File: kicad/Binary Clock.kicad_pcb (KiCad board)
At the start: 2 copper layers, 162.6 x 101.6 mm, 54 parts, among them J1 AVR-ISP-10, J2 UART, J3 COM/TWI, SW1 INC_HOUR, SW2 INC_MINUTE, SW3 INC_SECOND, SW4 INC_BTNESS, U1 PCF8583P, U2 ATmega32A-PU, Y1 32768hZ

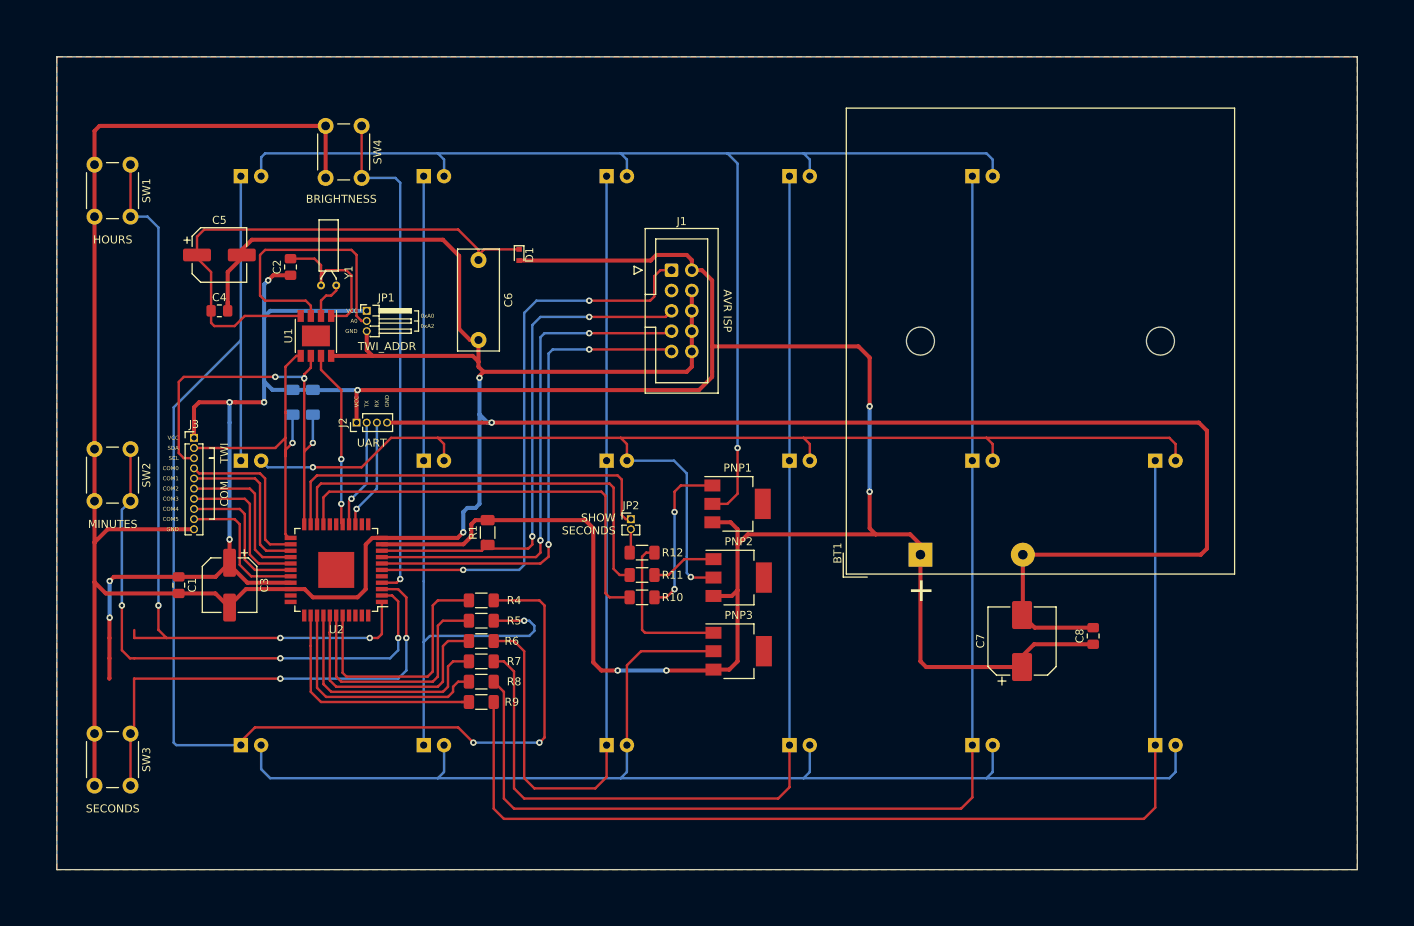
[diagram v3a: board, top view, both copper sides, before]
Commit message: Add support for buzzer
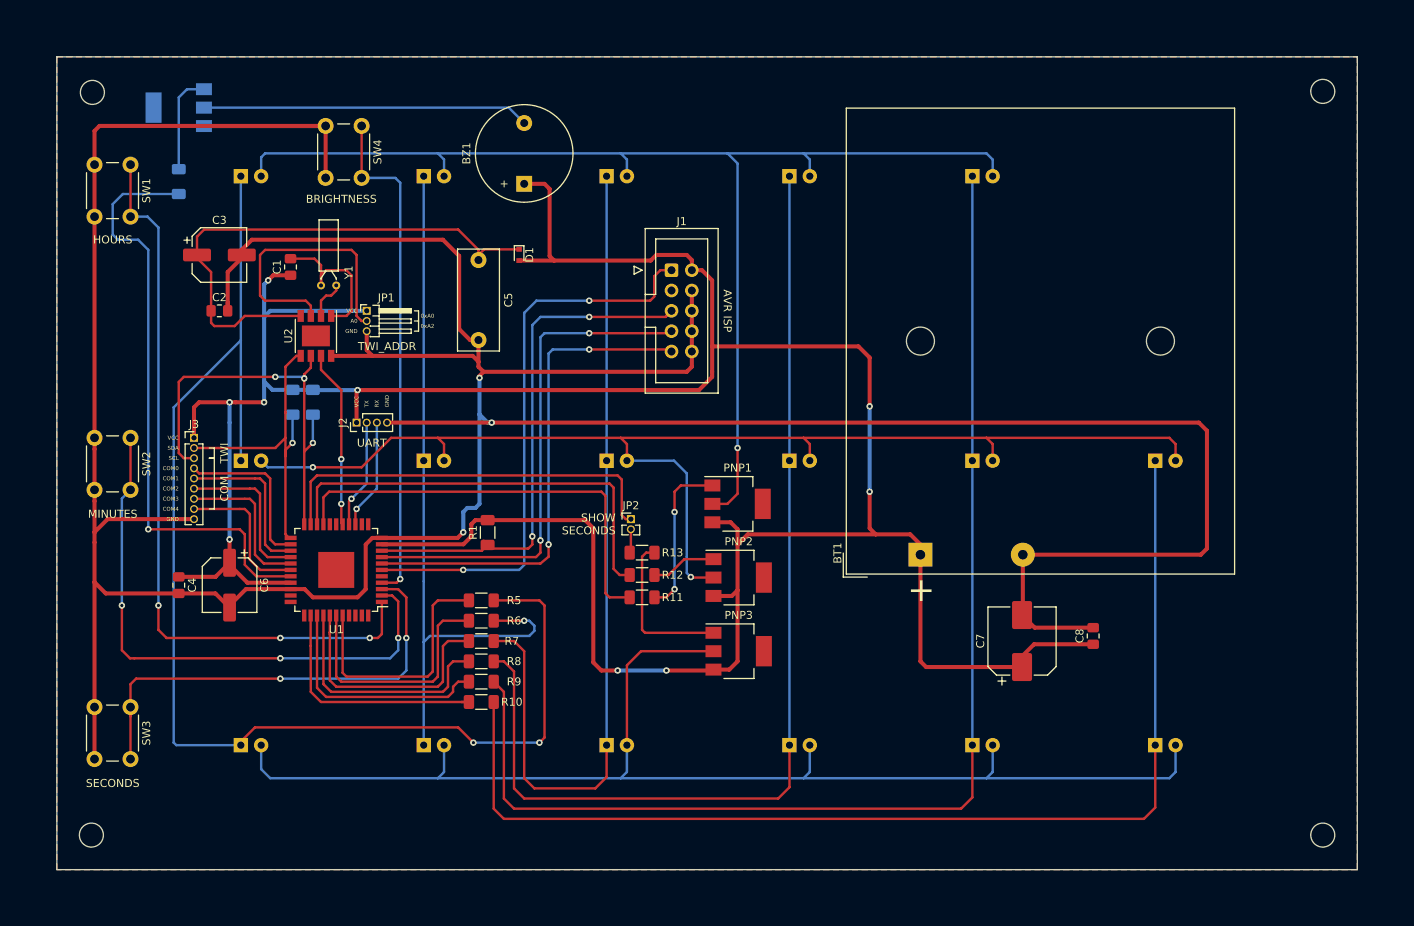
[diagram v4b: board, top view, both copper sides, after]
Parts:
- removed the C3 at (87.6, 121.9)
- added BZ1: Buzzer, Buzzer_Beeper:Buzzer_12x9.5RM7.6, F.Cu at (124.5, 71.8)
- added C6: 22u, Capacitor_SMD:CP_Elec_6.3x5.3, F.Cu at (87.6, 121.9)
- added NPN1: Q_NPN_BCE, Package_TO_SOT_SMD:SOT-223, B.Cu at (81.3, 62.2)
- added R4: 2k2, Resistor_SMD:R_1206_3216Metric_Pad1.30x1.75mm_HandSolder, B.Cu at (81.3, 71.5)
- added REF**: MountingHole_3mm, MountingHole:MountingHole_3mm, F.Cu at (224.3, 60.2)
- added REF**: MountingHole_3mm, MountingHole:MountingHole_3mm, F.Cu at (224.3, 153.2)
- added REF**: MountingHole_3mm, MountingHole:MountingHole_3mm, F.Cu at (70.4, 153.2)
- added REF**: MountingHole_3mm, MountingHole:MountingHole_3mm, F.Cu at (70.5, 60.3)
- J3: value COM/TWI -> COM/TW; footprint Connector_PinHeader_1.27mm:PinHeader_1x10_P1.27mm_Vertical -> Connector_PinHeader_1.27mm:PinHeader_1x09_P1.27mm_Vertical
- moved SW3 3.32 mm to (75.2, 137.2)
- moved SW2 1.41 mm to (75.2, 103.5)
- renumbered C2 to C1, C4 to C2, C5 to C3, C1 to C4, C6 to C5, R9 to R10, R10 to R11, R11 to R12, R12 to R13, R4 to R5, R5 to R6, R6 to R7, R7 to R8, R8 to R9, U2 to U1, U1 to U2
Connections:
- J3 pad 9: /COM5 -> GND
- U1 pad 29: /COM5 -> /BUZZER
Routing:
- net /BUZZER: track 0.00 -> 75.2 mm, vias 0 -> 1
- net Net-(BZ1-Pad2): track 0.00 -> 42.1 mm
- net /COM5: track 18.0 -> 0.00 mm
- net Net-(NPN1-Pad1): track 0.00 -> 12.5 mm
- net GND: track 480.6 -> 492.6 mm
- net VCC: track 394.9 -> 386.4 mm, vias 11 -> 9
- net /INC_HOUR: track 98.4 -> 93.4 mm
- net /INC_SECOND: track 60.6 -> 57.2 mm
- net /INC_MINUTE: track 69.4 -> 70.8 mm
- added copper zone on B.Cu, net (none)
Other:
- board text removed: "COM5"

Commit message: Change goldpins to 2.56mm
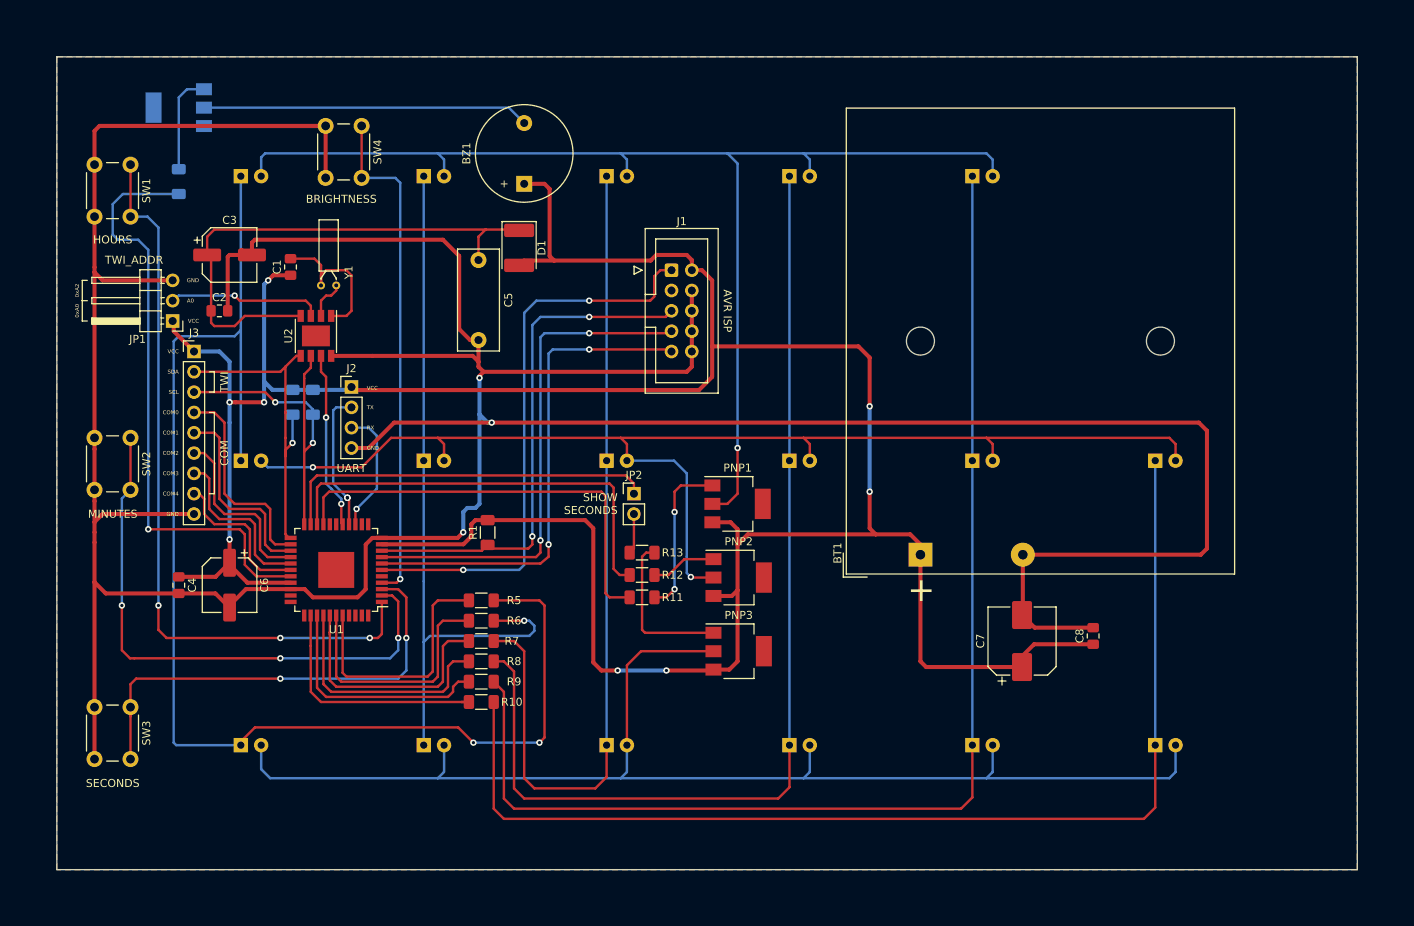
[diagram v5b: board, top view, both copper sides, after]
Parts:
- removed REF** (x4): MountingHole_3mm, MountingHole:MountingHole_3mm
- D1: footprint Diode_SMD:D_SOD-523 -> Diode_SMD:D_2114_3652Metric
- J2: footprint Connector_PinHeader_1.27mm:PinHeader_1x04_P1.27mm_Vertical -> Connector_PinHeader_2.54mm:PinHeader_1x04_P2.54mm_Vertical
- J3: footprint Connector_PinHeader_1.27mm:PinHeader_1x09_P1.27mm_Vertical -> Connector_PinHeader_2.54mm:PinHeader_1x09_P2.54mm_Vertical
- JP1: footprint Connector_PinHeader_1.27mm:PinHeader_1x03_P1.27mm_Horizontal -> Connector_PinHeader_2.54mm:PinHeader_1x03_P2.54mm_Horizontal
- JP2: footprint Connector_PinHeader_1.27mm:PinHeader_1x02_P1.27mm_Vertical -> Connector_PinHeader_2.54mm:PinHeader_1x02_P2.54mm_Vertical
- moved JP1 24.3 mm to (80.5, 88.9), turned to 180 degrees
- moved J3 10.8 mm to (83.2, 92.7)
- moved J2 4.49 mm to (102.9, 97.2), turned to 0 degrees
- moved JP2 3.20 mm to (138.2, 110.5)
- moved C3 1.27 mm to (87.6, 80.6)
- moved D1 0.89 mm to (123.8, 79.8)
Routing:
- net Net-(JP1-Pad2): track 35.0 -> 19.2 mm, vias 0 -> 1
- net GND: track 492.6 -> 506.4 mm
- net /SCL: track 53.9 -> 42.9 mm, vias 3 -> 2
- net VCC: track 386.4 -> 376.2 mm, vias 9 -> 8
- net /COM0: track 20.5 -> 26.3 mm
- net Net-(HD1-Pad1): track 162.0 -> 167.4 mm
- net /COM1: track 20.3 -> 24.9 mm
- net /TX: track 13.6 -> 17.5 mm, vias 1 -> 2
- net /COM2: track 19.7 -> 22.7 mm
- net /SECOND_LED: track 50.5 -> 47.8 mm
- net Net-(JP2-Pad2): track 3.02 -> 5.26 mm
- net /COM3: track 19.2 -> 21.2 mm
- net /RX: track 13.8 -> 15.8 mm
- net /COM4: track 18.6 -> 19.4 mm

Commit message: Update PCB footprints
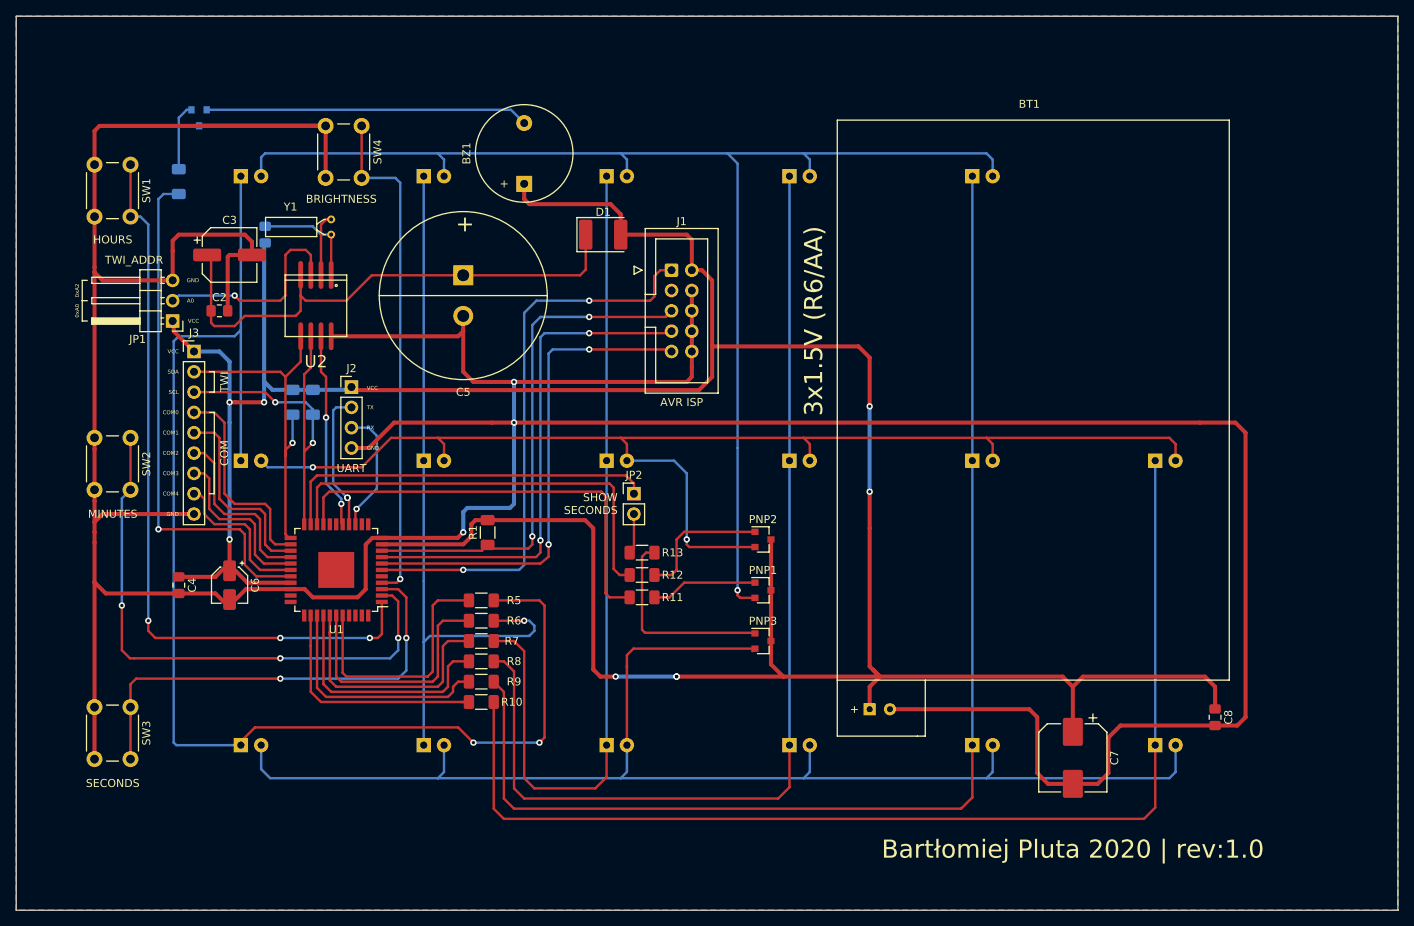
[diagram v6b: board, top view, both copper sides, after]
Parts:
- BT1: footprint Battery:BatteryHolder_TruPower_BH-331P_3xAA -> Project Footprints:BatteryPackage
- C1: moved to B.Cu
- C5: footprint Capacitor_THT:C_Disc_D12.5mm_W5.0mm_P10.00mm -> Project Footprints:SuperCapacitor
- C6: footprint Capacitor_SMD:CP_Elec_6.3x5.3 -> Capacitor_SMD:CP_Elec_4x3
- NPN1, PNP1, PNP2, PNP3: footprint Package_TO_SOT_SMD:SOT-223 -> Package_TO_SOT_SMD:SOT-23
- U2: footprint Package_SO:Diodes_SO-8EP -> PCF8583:SOT176-1
- moved BT1 25.0 mm to (188.6, 97.8), turned to 0 degrees
- moved C8 18.3 mm to (210.8, 138.4), turned to 270 degrees
- moved C7 15.9 mm to (193.0, 143.5), turned to 270 degrees
- moved PNP1 11.3 mm to (154.3, 122.6)
- moved D1 10.6 mm to (134.3, 78.1), turned to 0 degrees
- moved Y1 8.28 mm to (100.3, 76.2), turned to 270 degrees
- moved PNP2 5.65 mm to (154.3, 116.2)
- moved C1 5.14 mm to (92.1, 78.1)
- moved C5 4.84 mm to (116.8, 85.7)
- moved U2 3.77 mm to (98.4, 87.0), turned to 180 degrees
- moved PNP3 3.29 mm to (154.3, 128.9)
- moved NPN1 2.84 mm to (83.8, 63.5), turned to 270 degrees
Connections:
- J1 pad 3: Net-(J1-Pad3) -> (no net)
- U1 pad 12: Net-(U1-Pad12) -> (no net)
- U1 pad 13: Net-(U1-Pad13) -> (no net)
- U1 pad 17: Net-(U1-Pad17) -> (no net)
- U1 pad 18: Net-(U1-Pad18) -> (no net)
- U1 pad 32: Net-(U1-Pad32) -> (no net)
- U1 pad 33: Net-(U1-Pad33) -> (no net)
- U1 pad 34: Net-(U1-Pad34) -> (no net)
- U1 pad 5: Net-(U1-Pad5) -> (no net)
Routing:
- net GND: track 506.4 -> 532.5 mm
- net VCC: track 376.2 -> 397.0 mm
- net Net-(HD1-Pad2): track 152.7 -> 164.0 mm
- net /BUZZER: track 75.2 -> 65.3 mm
- net Net-(PNP2-Pad1): track 8.20 -> 17.0 mm
- net Net-(PNP1-Pad1): track 20.2 -> 13.3 mm, vias 2 -> 0
- net Net-(JP1-Pad2): track 19.2 -> 26.0 mm
- net Net-(PNP3-Pad2): track 160.8 -> 167.6 mm
- net Net-(C1-Pad2): track 19.5 -> 13.7 mm
- net Net-(PNP3-Pad1): track 20.0 -> 25.2 mm
- net Net-(NPN1-Pad1): track 12.5 -> 8.43 mm
- net Net-(U2-Pad2): track 4.97 -> 7.84 mm
- net /SCL: track 42.9 -> 45.3 mm
- net /RTC_INT: track 22.2 -> 24.6 mm
- net /SDA: track 41.5 -> 43.6 mm
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- added copper zone on B.Cu, net GND
- removed copper zone on B.Cu, net (none)
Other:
- board size 162.6 x 101.6 mm -> 172.7 x 111.8 mm
- board text added: "3x1.5V (R6/AA)"
- board text added: "Bartłomiej Pluta 2020 | rev:1.0"

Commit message: Fix some issues on PCB
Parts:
- added REF**: MountingHole_2mm, MountingHole:MountingHole_2mm, F.Cu at (160.0, 55.9)
- added REF**: MountingHole_2mm, MountingHole:MountingHole_2mm, F.Cu at (134.6, 55.9)
- added REF**: MountingHole_3mm, MountingHole:MountingHole_3mm, F.Cu at (228.6, 55.9)
- added REF**: MountingHole_3mm, MountingHole:MountingHole_3mm, F.Cu at (228.6, 157.5)
- added REF**: MountingHole_3mm, MountingHole:MountingHole_3mm, F.Cu at (66.0, 157.5)
- added REF**: MountingHole_3mm, MountingHole:MountingHole_3mm, F.Cu at (66.0, 55.9)
- NPN1: value Q_NPN_BCE -> Q_NPN_BEC
- PNP1, PNP2, PNP3: value Q_PNP_BCE -> Q_PNP_BEC
- R10, R5, R6, R7, R8, R9: value 56R -> 100R
- moved PNP2 5.85 mm to (160.0, 117.5)
- moved PNP3 5.85 mm to (160.0, 127.6)
- moved PNP1 5.72 mm to (160.0, 122.6)
- moved NPN1 3.42 mm to (85.1, 66.7), turned to 0 degrees
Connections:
- HD1 pad 2: Net-(HD1-Pad2) -> /HC
- HD2 pad 2: Net-(HD1-Pad2) -> /HC
- HD3 pad 2: Net-(HD1-Pad2) -> /HC
- HD4 pad 2: Net-(HD1-Pad2) -> /HC
- HD5 pad 2: Net-(HD1-Pad2) -> /HC
- MD1 pad 2: Net-(MD1-Pad2) -> /MC
- MD2 pad 2: Net-(MD1-Pad2) -> /MC
- MD3 pad 2: Net-(MD1-Pad2) -> /MC
- MD4 pad 2: Net-(MD1-Pad2) -> /MC
- MD5 pad 2: Net-(MD1-Pad2) -> /MC
- MD6 pad 2: Net-(MD1-Pad2) -> /MC
- NPN1 pad 2: Net-(BZ1-Pad2) -> GND
- NPN1 pad 3: GND -> Net-(BZ1-Pad2)
- PNP1 pad 2: Net-(HD1-Pad2) -> VCC
- PNP1 pad 3: VCC -> /HC
- PNP2 pad 2: Net-(MD1-Pad2) -> VCC
- PNP2 pad 3: VCC -> /MC
- PNP3 pad 2: Net-(PNP3-Pad2) -> VCC
- PNP3 pad 3: VCC -> /SC
- SD1 pad 2: Net-(PNP3-Pad2) -> /SC
- SD2 pad 2: Net-(PNP3-Pad2) -> /SC
- SD3 pad 2: Net-(PNP3-Pad2) -> /SC
- SD4 pad 2: Net-(PNP3-Pad2) -> /SC
- SD5 pad 2: Net-(PNP3-Pad2) -> /SC
- SD6 pad 2: Net-(PNP3-Pad2) -> /SC
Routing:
- net Net-(PNP3-Pad2): track 167.6 -> 0.00 mm
- net /HC: track 0.00 -> 165.0 mm, vias 0 -> 1
- net Net-(HD1-Pad2): track 164.0 -> 0.00 mm, vias 1 -> 0
- net Net-(MD1-Pad2): track 157.0 -> 0.00 mm, vias 2 -> 0
- net /SC: track 0.00 -> 156.9 mm, vias 0 -> 1
- net /MC: track 0.00 -> 142.7 mm, vias 0 -> 1
- net VCC: track 397.0 -> 410.8 mm, vias 8 -> 5
- net Net-(PNP1-Pad1): track 13.3 -> 19.0 mm
- net Net-(PNP3-Pad1): track 25.2 -> 29.4 mm
- net Net-(NPN1-Pad1): track 8.43 -> 4.54 mm
- net Net-(PNP2-Pad1): track 17.0 -> 20.0 mm
- net GND: track 532.5 -> 533.1 mm
- added copper zone on B.Cu, net VCC
- removed copper zone on B.Cu, net GND
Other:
- net class LED Collector added: clearance 0.2, trace_width 0.508, via_dia 0.8, via_drill 0.4
- rule trace_min: 0.2 -> 0.127
- rule via_min_size: 0.4 -> 0.254
